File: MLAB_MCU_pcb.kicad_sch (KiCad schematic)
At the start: 0 parts

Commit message: Collecting components and starting work on schematic
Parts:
- added C1, C2, C3, C4: 1u, Capacitor_SMD:C_0805_2012Metric_Pad1.18x1.45mm_HandSolder, symbol Device:C
- added J1, J2: Conn_01x02_Pin, Connector_PinHeader_2.54mm:PinHeader_1x02_P2.54mm_Vertical, symbol Connector:Conn_01x02_Pin
- added J3: Input Header, Connector_PinHeader_2.54mm:PinHeader_1x02_P2.54mm_Vertical, symbol Connector:Conn_01x02_Pin
- added J4: TBC05-02-1-G-G, TerminalBlock_Phoenix:TerminalBlock_Phoenix_MPT-0,5-2-2.54_1x02_P2.54mm_Horizontal, symbol Connector:Screw_Terminal_01x02
- added U1: TPS7A2012PDBVRG4, Package_TO_SOT_SMD:SOT-23-5, symbol Regulator_Linear:TPS7A20xxxDBV
- added U2: TPS7A2033PDBVR, Package_TO_SOT_SMD:SOT-23-5, symbol Regulator_Linear:TPS7A20xxxDBV
- added U3: DSC1101DL5-020.0000, 1_mlab_mcu_fp:VDFN6_2P5X2_MCH, symbol 1_mlab_mcu:DSC1101DL5-020.0000
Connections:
- new net: C2.1, J1.2 (Pin_2), U1.5 (OUT)
- new net: C1.1, J3.1 (Pin_1), J4.2 (Pin_2), U1.1 (IN), U1.3 (EN)
- new net: C3.1, J3.2 (Pin_2), J4.1 (Pin_1), U2.1 (IN), U2.3 (EN)
- new net: C4.1, J2.2 (Pin_2), U2.5 (OUT)
- new net 0: C1.2, C2.2, C3.2, C4.2, U1.2 (GND), U2.2 (GND)

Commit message: Schematic WIP
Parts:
- added C5, C6, C7, C8, C9: 0.1u, Capacitor_SMD:C_0805_2012Metric_Pad1.18x1.45mm_HandSolder, symbol Device:C
- added D1, D10, D2, D3, D4, D5, D6, D7, D8, D9: LED, LED_SMD:LED_0805_2012Metric_Pad1.15x1.40mm_HandSolder, symbol Device:LED
- added IC1: (no value), 1_mlab_mcu_fp:VQFN-32-1EP_5x5mm_P0.5mm_EP3.5x3.5mm, symbol 1_mlab_mcu:mlab_mcu
- added J10, J11, J12, J13, J14, J15, J16, J17, J7, J8, J9: Conn_01x02_Pin, Connector_PinHeader_2.54mm:PinHeader_1x02_P2.54mm_Vertical, symbol Connector:Conn_01x02_Pin
- added J5: 232-5205-01, 1_mlab_mcu_fp:CONN_232-5205-01_3MM, symbol 1_mlab_mcu:232-5205-01
- added J6: Conn_Coaxial, Connector_Coaxial:SMA_Amphenol_132134_Vertical, symbol Connector:Conn_Coaxial
- added R1, R2, R3: 1, Resistor_SMD:R_0805_2012Metric_Pad1.20x1.40mm_HandSolder, symbol Device:R
- added R10, R11, R8, R9: 4.7k, Resistor_SMD:R_0805_2012Metric_Pad1.20x1.40mm_HandSolder, symbol Device:R
- added R12, R13, R14, R15, R16, R17, R18, R19, R20, R21: 30, Resistor_SMD:R_0805_2012Metric_Pad1.20x1.40mm_HandSolder, symbol Device:R
- added R22, R23, R24, R25, R26, R27, R28, R29, R30, R31: 1k, Resistor_SMD:R_0805_2012Metric_Pad1.20x1.40mm_HandSolder, symbol Device:R
- added R4: 50, Resistor_SMD:R_0805_2012Metric_Pad1.20x1.40mm_HandSolder, symbol Device:R
- added R5, R6, R7: 10k, Resistor_SMD:R_0805_2012Metric_Pad1.20x1.40mm_HandSolder, symbol Device:R
- added U4: 24LC512, Package_DIP:DIP-8_W7.62mm_Socket, symbol Memory_EEPROM:24LC512
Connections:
- net 0: now also U3.3 (GND), C5.2, C6.2, C7.2, C8.2, C9.2, D1.1 (K), D10.1 (K), D2.1 (K), D3.1 (K), D4.1 (K), D5.1 (K), D6.1 (K), D7.1 (K), D8.1 (K), D9.1 (K), J6.2 (Ext), R3.1, R4.1, R5.2, U4.4 (GND)
- net at U3.4 (OUT): now also J7.2 (Pin_2)
- net +3V3: now reaches U3.6 (VDD)
- net +3V3: now also J2.1 (Pin_1), C5.1, C7.1, C9.1, R10.1, R11.1, R2.2, R6.1, R8.1, R9.1, U4.8 (VCC)
- net +1V2: now reaches J1.1 (Pin_1)
- net +1V2: now also C6.1, R1.1
- new net: J10.1 (Pin_1), R24.1
- new net: J10.2 (Pin_2), R14.2
- new net: J8.1 (Pin_1), R22.1
- new net: J8.2 (Pin_2), R12.2
- new net: IC1.14 (VSS), IC1.15 (VSS), IC1.16 (VSS), IC1.17 (VSS), IC1.19 (VSS), IC1.25 (VSS), IC1.3 (VSS), IC1.30 (VSS), IC1.31 (VSS), IC1.32 (VSS), IC1.8 (VSS), IC1.9 (VSS), R3.2
- new net: J11.1 (Pin_1), R25.1
- new net: D4.2 (A), R25.2
- new net: J15.2 (Pin_2), R19.2
- new net: D3.2 (A), R24.2
- new net: J9.1 (Pin_1), R23.1
- new net: J9.2 (Pin_2), R13.2
- new net: D5.2 (A), R26.2
- new net: J16.2 (Pin_2), R20.2
- new net: D9.2 (A), R30.2
- new net: D8.2 (A), R29.2
- new net: J11.2 (Pin_2), R15.2
- new net: IC1.23 (VDD_CORE), IC1.4 (VDD_CORE), R1.2
- new net: J12.1 (Pin_1), R26.1
- new net: J12.2 (Pin_2), R16.2
- new net: J16.1 (Pin_1), R30.1
- new net: J15.1 (Pin_1), R29.1
- new net: D7.2 (A), R28.2
- new net: IC1.21 (test_mode), R5.1
- new net: J14.1 (Pin_1), R28.1
- new net: J14.2 (Pin_2), R18.2
- new net: D1.2 (A), R22.2
- new net: J17.1 (Pin_1), R31.1
- new net: J17.2 (Pin_2), R21.2
- new net: D2.2 (A), R23.2
- new net: IC1.10 (VDD_IO), IC1.24 (VDD_IO), IC1.26 (VDD_IO), R2.1
- new net: D6.2 (A), R27.2
- new net: J13.2 (Pin_2), R17.2
- new net: D10.2 (A), R31.2
- new net: J13.1 (Pin_1), R27.1
- new net GPIO0: IC1.27 (GPIO_0), R12.1
- new net GPIO1: IC1.28 (GPIO_1), R13.1
- new net GPIO2: IC1.29 (GPIO_2), R14.1
- new net GPIO3: IC1.1 (GPIO_3), R15.1
- new net GPIO4: IC1.2 (GPIO_4), R16.1
- new net GPIO5: IC1.5 (GPIO_5), R17.1
- new net GPIO6: IC1.6 (GPIO_6), R18.1
- new net GPIO7: IC1.7 (GPIO_7), R19.1
- new net GPIO8: IC1.11 (GPIO_8), R20.1
- new net GPIO9: IC1.18 (GPIO_9), R21.1
- new net SCL: IC1.12 (SCL), R10.2, R11.2, U4.6 (SCL)
- new net SDA: IC1.13 (SDA), R8.2, R9.2, U4.5 (SDA)
- new net clk: IC1.20 (clk), J6.1 (In), J7.1 (Pin_1), R4.2
- new net rst: C8.1, IC1.22 (rst_n), R6.2, R7.2
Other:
- note added: "4-6V Power input"
- note added: "50 Ohm shunt for SMA, is this necessary?"
- note added: "High-side shunts for seperate IO and CORE power measurements (use diff probes)"
- note added: "NC on EN means Output Active"
- note added: "Select 20MHz CMOS Osc or external clk gen from SMA can also connect slow scan clock from FPGA directly to this header"
- note added: "Select between LDO and bench supply"
- moved on the sheet: C1, C2, C3, C4, J1, J2, J3, J4, U1, U2

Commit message: Schematic still WIP
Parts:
- added C10, C11: 1u, Capacitor_SMD:C_0805_2012Metric_Pad1.18x1.45mm_HandSolder, symbol Device:C
- added J18, J19: Conn_02x05_Odd_Even, Connector_PinHeader_2.54mm:PinHeader_2x05_P2.54mm_Vertical, symbol Connector_Generic:Conn_02x05_Odd_Even
- added S1: SWS065-030V12TSK_REVA, 1_mlab_mcu_fp:SW_SWS065-030V12TSK_REVA, symbol 1_mlab_mcu:SWS065-030V12TSK_REVA
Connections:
- net +1V2: now also C10.1
- net +3V3: now also C11.1
- net 0: now also R5.1, U4.1 (A0), U4.2 (A1), U4.3 (A2), U4.7 (WP), C10.2, C11.2, J18.10 (Pin_10), J18.9 (Pin_9), J19.10 (Pin_10), J19.9 (Pin_9), S1.3, S1.SH1 (SHIELD), S1.SH2 (SHIELD); no longer R5.2
- net GPIO0: now also J5.27, J18.6 (Pin_6)
- net GPIO1: now also J5.28, J18.4 (Pin_4)
- net GPIO2: now also J5.29, J19.8 (Pin_8); no longer IC1.29 (GPIO_2)
- net GPIO3: now also J5.1, J19.6 (Pin_6)
- net GPIO4: now also J5.2, J19.4 (Pin_4)
- net GPIO5: now also J5.5, J19.2 (Pin_2)
- net GPIO6: now also J5.6, J19.7 (Pin_7)
- net GPIO7: now also J5.7, J19.5 (Pin_5)
- net GPIO8: now also J5.11, J19.3 (Pin_3)
- net GPIO9: now also J5.18, J19.1 (Pin_1)
- net SCL: now also J5.12, J18.8 (Pin_8)
- net SDA: now also J5.13, J18.7 (Pin_7)
- net clk: now also J5.20, J18.1 (Pin_1)
- net rst: now also J5.22, J18.3 (Pin_3); no longer R6.2
- net VSS: now reaches IC1.14 (VSS), IC1.15 (VSS), IC1.16 (VSS), IC1.17 (VSS), IC1.19 (VSS), IC1.25 (VSS), IC1.3 (VSS), IC1.30 (VSS), IC1.31 (VSS), IC1.32 (VSS), IC1.8 (VSS), IC1.9 (VSS), R3.2
- net VSS: now also J5.14, J5.15, J5.16, J5.17, J5.19, J5.25, J5.3, J5.30, J5.31, J5.32, J5.8, J5.9
- net at R7.1: now also R6.2, S1.1, S1.2
- net VDD_CORE: now reaches IC1.23 (VDD_CORE), IC1.4 (VDD_CORE), R1.2
- net VDD_CORE: now also J5.23, J5.4
- net TM: now reaches IC1.21 (test_mode)
- net TM: now also J5.21, R5.2, J18.5 (Pin_5); no longer R5.1
- net VDD_IO: now reaches IC1.10 (VDD_IO), IC1.24 (VDD_IO), IC1.26 (VDD_IO), R2.1
- net VDD_IO: now also J5.10, J5.24, J5.26
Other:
- note added: "All address pins to GND as in FPGA test, writing enabled"
- note added: "Clock"
- note added: "EEPROM"
- note added: "For fast mode SCL=400kHz pull-up should be 2kOhm, so connect both 4.7k resistors"
- note added: "GPIO"
- note added: "Headers for FPGA"
- note added: "MCU"
- note added: "Reset"
- note added: "Socket"
- note added: "Supply generation"
- note added: "Use IDC ribbon to conect to FPGA PMOD"
- moved on the sheet: C1, C2, C3, C4, C5, C6, C7, C8, C9, D1, D10, D2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

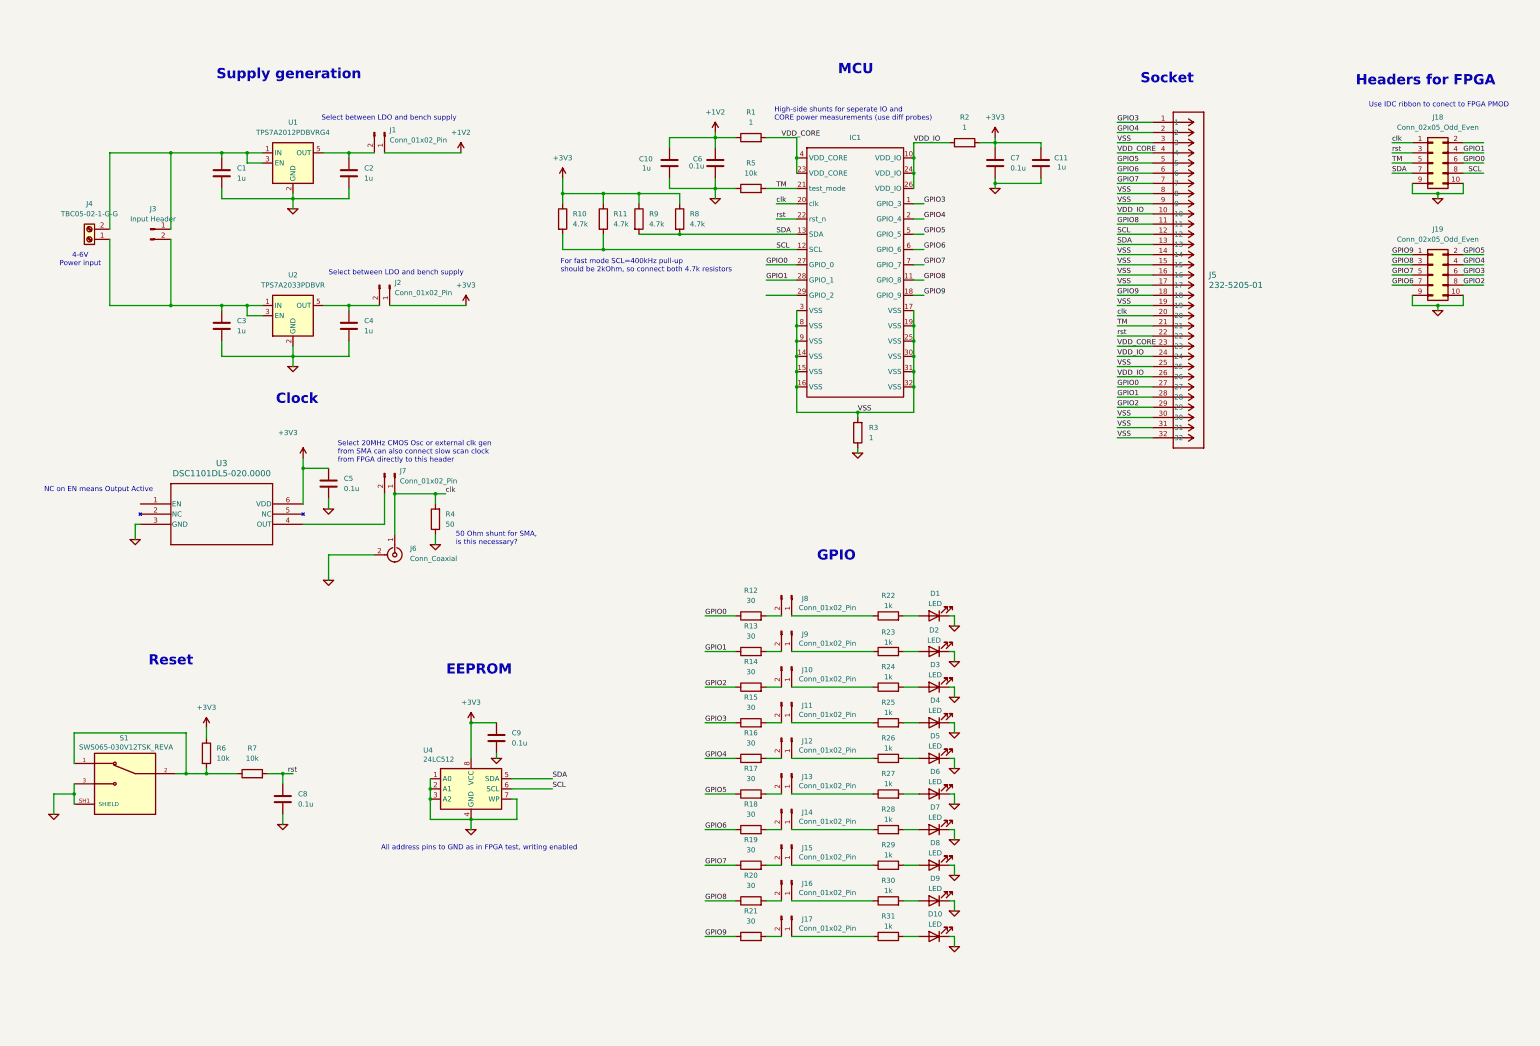
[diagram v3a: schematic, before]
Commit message: Schematic done
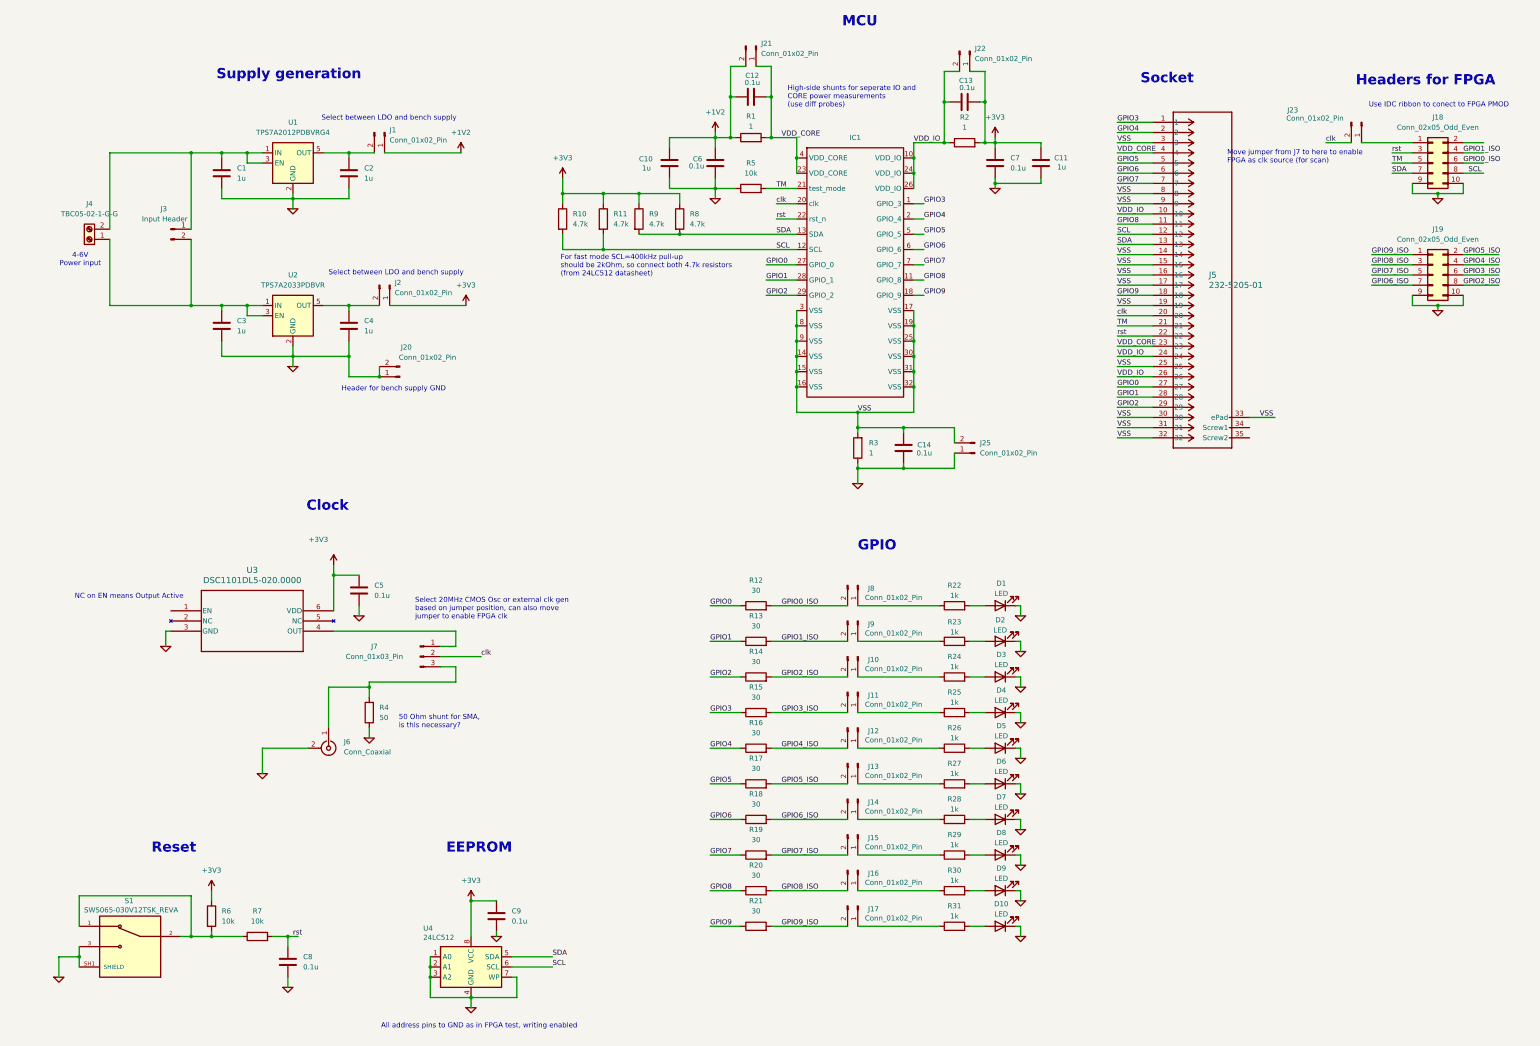
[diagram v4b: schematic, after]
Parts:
- removed J7: Conn_01x02_Pin, Connector_PinHeader_2.54mm:PinHeader_1x02_P2.54mm_Vertical, symbol Connector:Conn_01x02_Pin
- added C12, C13, C14: 0.1u, Capacitor_SMD:C_0805_2012Metric_Pad1.18x1.45mm_HandSolder, symbol Device:C
- added J20, J21, J22, J23, J25: Conn_01x02_Pin, Connector_PinHeader_2.54mm:PinHeader_1x02_P2.54mm_Vertical, symbol Connector:Conn_01x02_Pin
- added J7: Conn_01x03_Pin, Connector_PinHeader_2.54mm:PinHeader_1x03_P2.54mm_Vertical, symbol Connector:Conn_01x03_Pin
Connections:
- net +1V2: now also C12.1, J21.2 (Pin_2)
- net +3V3: now also C13.2, J22.1 (Pin_1)
- net 0: now also C14.1, J20.1 (Pin_1), J20.2 (Pin_2), J25.1 (Pin_1)
- net GPIO0: no longer J18.6 (Pin_6)
- net GPIO1: no longer J18.4 (Pin_4)
- net GPIO2: now also IC1.29 (GPIO_2); no longer J19.8 (Pin_8)
- net GPIO3: no longer J19.6 (Pin_6)
- net GPIO4: no longer J19.4 (Pin_4)
- net GPIO5: no longer J19.2 (Pin_2)
- net GPIO6: no longer J19.7 (Pin_7)
- net GPIO7: no longer J19.5 (Pin_5)
- net GPIO8: no longer J19.3 (Pin_3)
- net GPIO9: no longer J19.1 (Pin_1)
- net VDD_CORE: now also C12.2, J21.1 (Pin_1)
- net VDD_IO: now also C13.1, J22.2 (Pin_2)
- net VSS: now also J5.33 (ePad), C14.2, J25.2 (Pin_2)
- net clk: now also J23.2 (Pin_2), J7.2 (Pin_2); no longer J18.1 (Pin_1), J6.1 (In), R4.2
- net GPIO2_ISO: now reaches J10.2 (Pin_2), R14.2
- net GPIO2_ISO: now also J19.8 (Pin_8)
- net GPIO0_ISO: now reaches J8.2 (Pin_2), R12.2
- net GPIO0_ISO: now also J18.6 (Pin_6)
- net GPIO7_ISO: now reaches J15.2 (Pin_2), R19.2
- net GPIO7_ISO: now also J19.5 (Pin_5)
- net GPIO1_ISO: now reaches J9.2 (Pin_2), R13.2
- net GPIO1_ISO: now also J18.4 (Pin_4)
- net GPIO8_ISO: now reaches J16.2 (Pin_2), R20.2
- net GPIO8_ISO: now also J19.3 (Pin_3)
- net GPIO3_ISO: now reaches J11.2 (Pin_2), R15.2
- net GPIO3_ISO: now also J19.6 (Pin_6)
- net GPIO4_ISO: now reaches J12.2 (Pin_2), R16.2
- net GPIO4_ISO: now also J19.4 (Pin_4)
- net GPIO6_ISO: now reaches J14.2 (Pin_2), R18.2
- net GPIO6_ISO: now also J19.7 (Pin_7)
- net GPIO9_ISO: now reaches J17.2 (Pin_2), R21.2
- net GPIO9_ISO: now also J19.1 (Pin_1)
- net at U3.4 (OUT): now also J7.1 (Pin_1)
- net GPIO5_ISO: now reaches J13.2 (Pin_2), R17.2
- net GPIO5_ISO: now also J19.2 (Pin_2)
- new net: J6.1 (In), J7.3 (Pin_3), R4.2
- new net: J18.1 (Pin_1), J23.1 (Pin_1)
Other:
- note added: "For fast mode SCL=400kHz pull-up should be 2kOhm, so connect both 4.7k resistors (from 24LC512 datasheet)"
- note added: "Header for bench supply GND"
- note added: "Move jumper from J7 to here to enable FPGA as clk source (for scan)"
- note added: "Select 20MHz CMOS Osc or external clk gen based on jumper position, can also move jumper to enable FPGA clk"
- note removed: "For fast mode SCL=400kHz pull-up should be 2kOhm, so connect both 4.7k resistors"
- note removed: "Select 20MHz CMOS Osc or external clk gen from SMA can also connect slow scan clock from FPGA directly to this header"
- moved on the sheet: C5, C8, C9, D1, D10, D2, D3, D4, D5, D6, D7, D8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

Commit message: Add Current-sense amps for all shunts
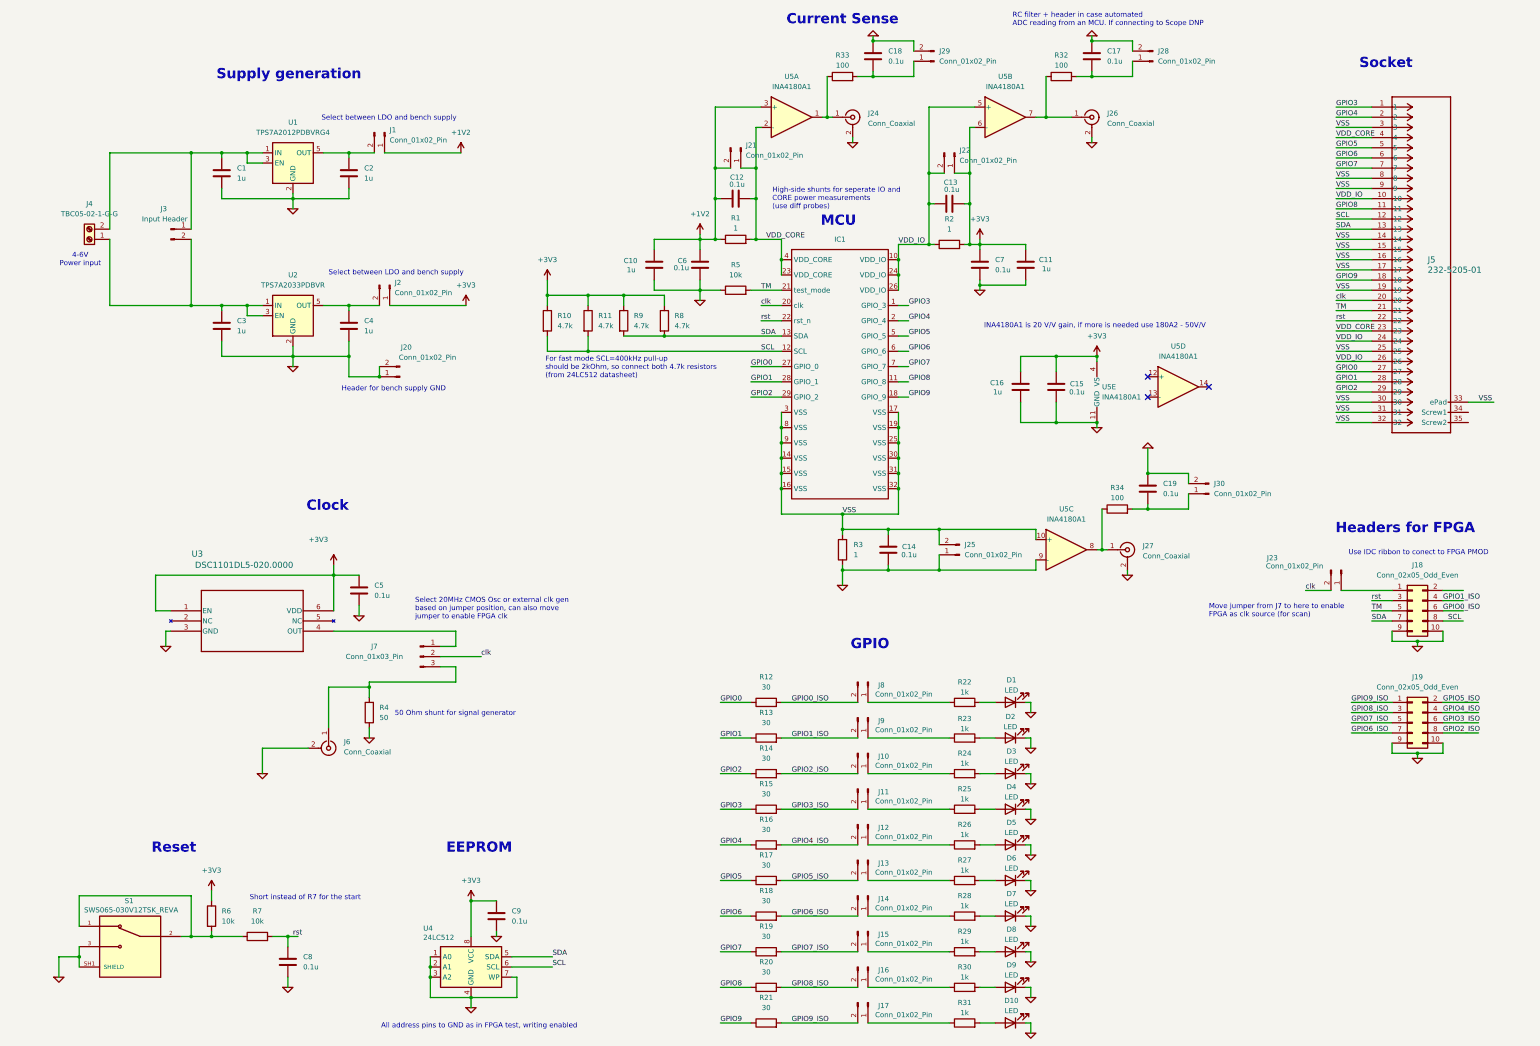
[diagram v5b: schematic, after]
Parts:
- added C15, C17, C18, C19: 0.1u, Capacitor_SMD:C_0805_2012Metric_Pad1.18x1.45mm_HandSolder, symbol Device:C
- added C16: 1u, Capacitor_SMD:C_0805_2012Metric_Pad1.18x1.45mm_HandSolder, symbol Device:C
- added J24, J26, J27: Conn_Coaxial, Connector_Coaxial:SMA_Amphenol_132134_Vertical, symbol Connector:Conn_Coaxial
- added J28, J29, J30: Conn_01x02_Pin, Connector_PinHeader_2.54mm:PinHeader_1x02_P2.54mm_Vertical, symbol Connector:Conn_01x02_Pin
- added R32, R33, R34: 100, Resistor_SMD:R_0805_2012Metric_Pad1.20x1.40mm_HandSolder, symbol Device:R
- added U5: INA4180A1, Package_SO:TSSOP-14_4.4x5mm_P0.65mm, symbol Amplifier_Current:INA4180A1
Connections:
- net +1V2: now also U5.3 (+)
- net +3V3: now also U3.1 (EN), C15.2, C16.1, U5.4 (VS), U5.6 (-)
- net 0: now also C15.1, C16.2, C17.2, C18.2, C19.2, J24.2 (Ext), J26.2 (Ext), J27.2 (Ext), J28.2 (Pin_2), J29.2 (Pin_2), J30.2 (Pin_2), U5.11 (GND), U5.9 (-)
- net VDD_CORE: now also U5.2 (-)
- net VDD_IO: now also U5.5 (+)
- net VSS: now also U5.10 (+)
- new net: J27.1 (In), R34.1, U5.8
- new net: C19.1, J30.1 (Pin_1), R34.2
- new net: J24.1 (In), R33.1, U5.1
- new net: C18.1, J29.1 (Pin_1), R33.2
- new net: J26.1 (In), R32.1, U5.7
- new net: C17.1, J28.1 (Pin_1), R32.2
- no-connect marks 0 -> 3
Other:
- note added: "50 Ohm shunt for signal generator"
- note added: "Current Sense"
- note added: "INA4180A1 is 20 V/V gain, if more is needed use 180A2 - 50V/V"
- note added: "RC filter + header in case automated ADC reading from an MCU. If connecting to Scope DNP"
- note added: "Short instead of R7 for the start"
- note removed: "50 Ohm shunt for SMA, is this necessary?"
- note removed: "NC on EN means Output Active"
- moved on the sheet: C10, C11, C12, C13, C14, C6, C7, D1, D10, D2, D3, D4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
